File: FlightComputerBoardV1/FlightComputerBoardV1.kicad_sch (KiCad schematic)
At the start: 0 parts

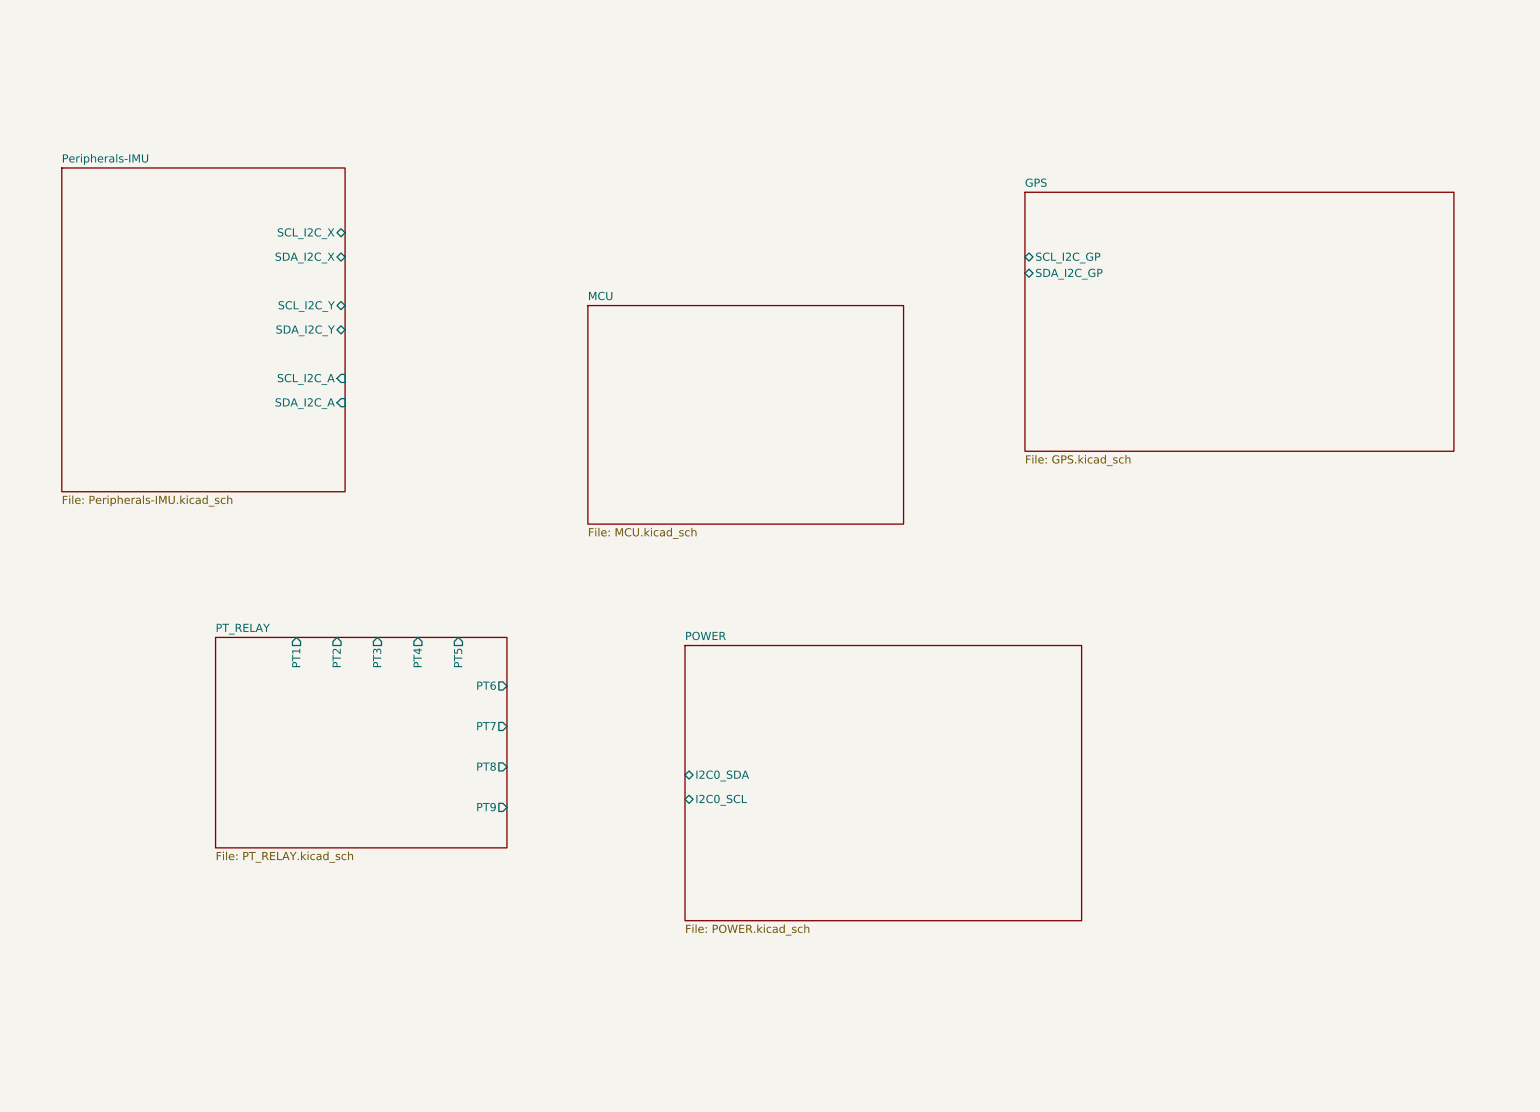
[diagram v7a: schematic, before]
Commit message: Addition to MCU sheet and peripheral connection complete
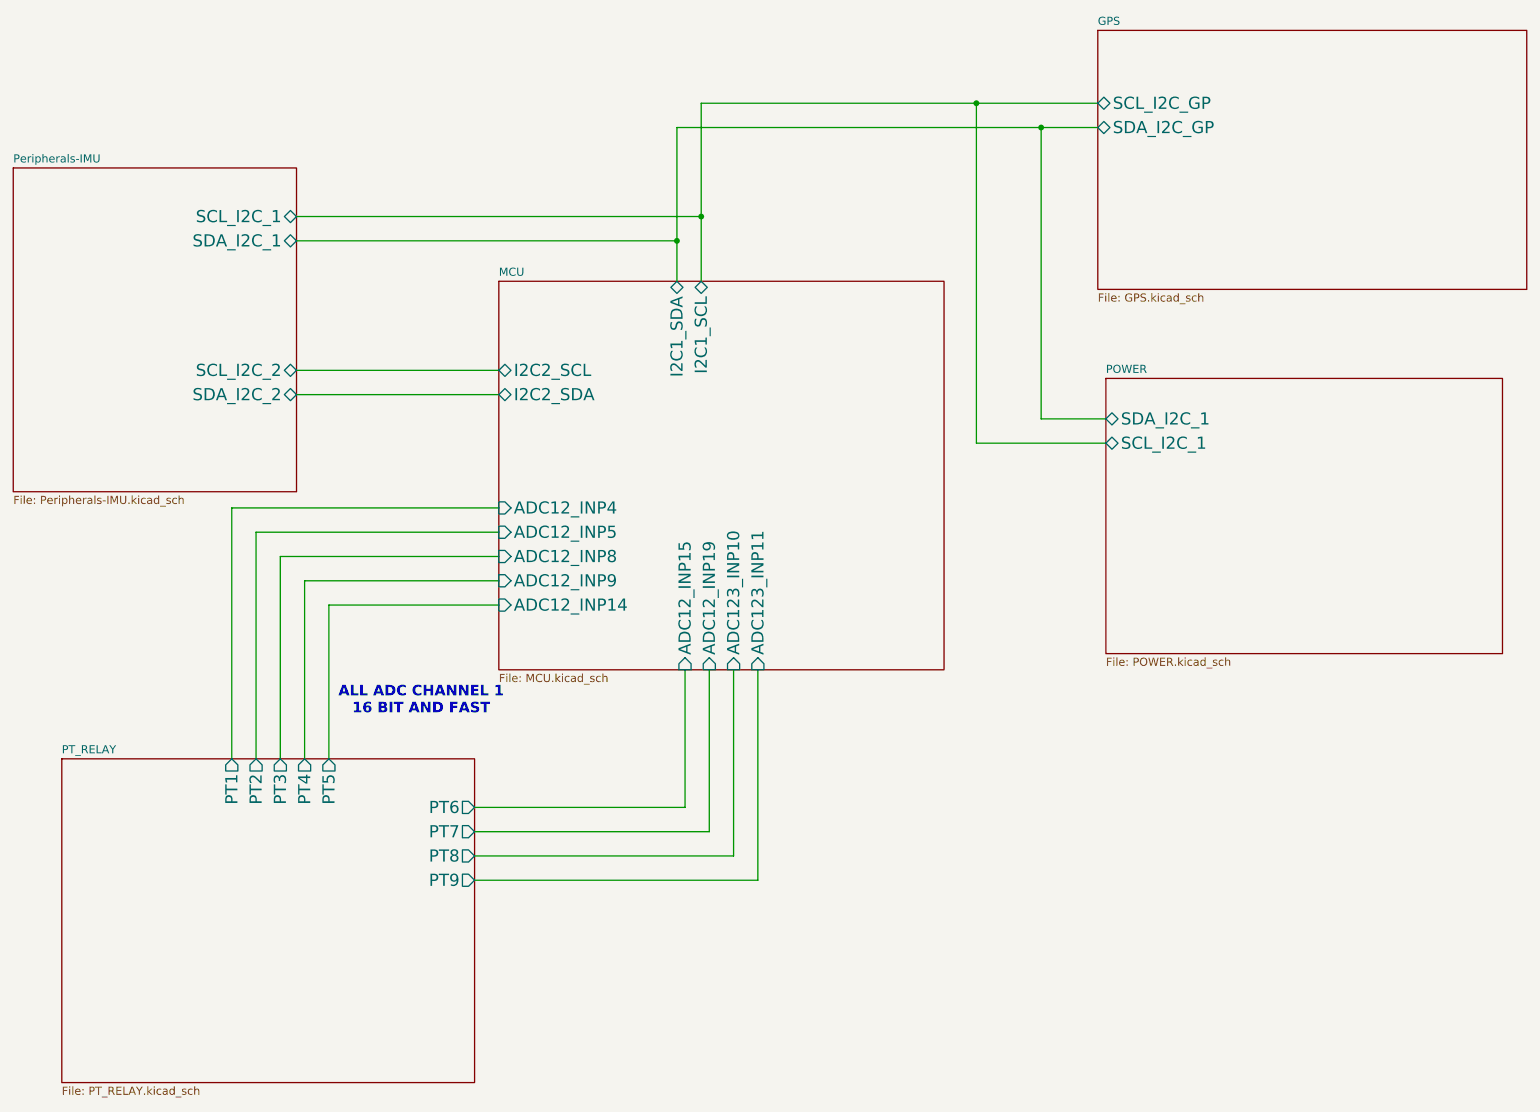
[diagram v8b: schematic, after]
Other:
- sheet MCU ports: added ADC123_INP10, ADC123_INP11, ADC12_INP14, ADC12_INP15, ADC12_INP19, ADC12_INP4, ADC12_INP5, ADC12_INP8, ADC12_INP9, I2C1_SCL, I2C1_SDA, I2C2_SCL, I2C2_SDA; removed none
- sheet POWER ports: added SCL_I2C_1, SDA_I2C_1; removed I2C0_SCL, I2C0_SDA
- sheet Peripherals-IMU ports: added SCL_I2C_1, SCL_I2C_2, SDA_I2C_1, SDA_I2C_2; removed SCL_I2C_A, SCL_I2C_X, SCL_I2C_Y, SDA_I2C_A, SDA_I2C_X, SDA_I2C_Y
- note added: "ALL ADC CHANNEL 1 16 BIT AND FAST"
